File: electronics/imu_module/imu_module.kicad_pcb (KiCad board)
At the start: 2 copper layers, 30 x 40 mm, 26 parts, among them J1 Conn_01x06_Male, J2 Conn_01x04, J3 Conn_01x04, SW1 SW_Push, SW2 SW_Push, SW3 SW_Push, U1 ESP32-WROOM-32U, U2 SP485, U3 ISM330DHCXTR, U4 SN74LV1T34DBVR, U5 AP2114HA-3.3TRG1

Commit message: hacky
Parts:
- removed the C4 at (19.0, 20.5)
- removed the C5 at (18.5, 16.0)
- removed the C8 at (26.0, 9.00)
- removed SW1, SW2, SW3: SW_Push, Button_Switch_SMD:SW_SPST_B3S-1000
- removed the U3 at (26.0, 15.0)
- added C1: 100n, Capacitor_SMD:C_0805_2012Metric, F.Cu at (22.2, 12.9)
- added C3: 100n, Capacitor_SMD:C_0805_2012Metric, F.Cu at (28.6, 13.8)
- added C6: 10u/50V, Capacitor_SMD:C_1206_3216Metric, B.Cu at (9.53, 24.5)
- added C9: 22u/16v, Capacitor_SMD:C_1206_3216Metric, B.Cu at (20.2, 5.00)
- added D1: WS2812B, lib:LED_WS2812B_PLCC4_5.0x5.0mm_P3.2mm_marked, B.Cu at (5.50, 30.0)
- added D2: WS2812B, lib:LED_WS2812B_PLCC4_5.0x5.0mm_P3.2mm_marked, B.Cu at (15.0, 30.0)
- added D3: WS2812B, lib:LED_WS2812B_PLCC4_5.0x5.0mm_P3.2mm_marked, B.Cu at (24.5, 30.0)
- added G***: LOGO, bitbots:bitbots_logo, B.Cu at (21.8, 12.3)
- added J2: Conn_01x03_Male, Connector_PinHeader_2.54mm:PinHeader_1x03_P2.54mm_Vertical, F.Cu at (28.0, 18.9)
- added JP1: SolderJumper_2_Open, Jumper:SolderJumper-2_P1.3mm_Open_RoundedPad1.0x1.5mm, F.Cu at (25.4, 9.60)
- added L1: 22uH, lib:VLS5045EX330M, B.Cu at (15.0, 4.70)
- added R2: 4K7, Resistor_SMD:R_0805_2012Metric, F.Cu at (8.59, 32.5)
- added R3: 4K7, Resistor_SMD:R_0805_2012Metric, F.Cu at (4.84, 32.5)
- added U2: BMI088, lib:PQFN50P450X300X100-16N, F.Cu at (25.4, 13.5)
- C10: renamed from C9; footprint Capacitor_SMD:C_0805_2012Metric_Pad1.15x1.40mm_HandSolder -> Capacitor_SMD:C_1206_3216Metric; moved to B.Cu
- C11: renamed from C10; footprint Capacitor_SMD:C_0805_2012Metric_Pad1.15x1.40mm_HandSolder -> Capacitor_SMD:C_1206_3216Metric; moved to B.Cu
- C2: renamed from C1; footprint Capacitor_SMD:C_0805_2012Metric_Pad1.15x1.40mm_HandSolder -> Capacitor_SMD:C_0805_2012Metric
- C4: renamed from C2; footprint Capacitor_SMD:C_0805_2012Metric_Pad1.15x1.40mm_HandSolder -> Capacitor_SMD:C_0805_2012Metric
- C5: renamed from C3; footprint Capacitor_SMD:C_0805_2012Metric_Pad1.15x1.40mm_HandSolder -> Capacitor_SMD:C_0805_2012Metric
- C7: value 100n -> 22u/16v; footprint Capacitor_SMD:C_0805_2012Metric_Pad1.15x1.40mm_HandSolder -> Capacitor_SMD:C_1206_3216Metric
- C8: renamed from C6; footprint Capacitor_SMD:C_0805_2012Metric_Pad1.15x1.40mm_HandSolder -> Capacitor_SMD:C_0805_2012Metric
- PS1: value VXO7805-500-M -> PXO7805-500-M-TR; footprint bitbots:VXO7805-500-M -> lib:CONV_PXO7805-500-M-TR
- R1: footprint Resistor_SMD:R_0805_2012Metric_Pad1.15x1.40mm_HandSolder -> Resistor_SMD:R_0805_2012Metric
- U5: moved to B.Cu
- moved C7 21.4 mm to (9.75, 5.00), turned to 90 degrees
- moved J1 15.8 mm to (17.7, 28.0), turned to 180 degrees
- moved C11 10.5 mm to (15.5, 24.8), turned to 90 degrees
- moved J4 8.16 mm to (10.2, 36.5), turned to 180 degrees
- moved C10 8.15 mm to (21.0, 17.6), turned to 180 degrees
- moved C5 7.57 mm to (17.5, 4.20), turned to 90 degrees
- moved U5 7.56 mm to (21.2, 22.9), turned to 180 degrees
- moved J3 7.49 mm to (27.4, 36.5), turned to 180 degrees
- moved C2 6.67 mm to (13.4, 2.75)
- moved C4 4.10 mm to (20.0, 4.20), turned to 90 degrees
- moved R1 3.51 mm to (13.3, 5.25), turned to 180 degrees
- moved PS1 2.06 mm to (9.35, 15.6)
- moved U3 1.95 mm to (23.7, 23.7), turned to 180 degrees
- moved U1 1.61 mm to (11.1, 16.8), turned to -90 degrees
- moved C8 1.50 mm to (22.5, 30.0), turned to -90 degrees
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- renumbered J2 to J3, J3 to J4, U4 to U3, U2 to U4
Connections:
- C7 pad 1: +3V3 -> Net-(PS1-+VO)
- J3 pad 1: GND -> DATA-
- J3 pad 2: +1V2 -> DATA+
- J3 pad 3: DATA+ -> VBUS
- J3 pad 4: DATA- -> GND
- J4 pad 1: GND -> DATA-
- J4 pad 2: +1V2 -> DATA+
- J4 pad 3: DATA+ -> VBUS
- J4 pad 4: DATA- -> GND
- PS1 pad 1: +1V2 -> VBUS
- PS1 pad 2: GND -> (no net)
- PS1 pad 3: +5V -> Net-(PS1-+VO)
- PS1 pad 4: Net-(PS1-Pad4) -> GND
- U1 pad 10: Net-(U1-Pad10) -> int1_accel
- U1 pad 11: Net-(U1-Pad11) -> SPI_CS_ACCEL
- U1 pad 12: Net-(U1-Pad12) -> unconnected-(U1-IO27-Pad12)
- U1 pad 13: INT_ACC -> unconnected-(U1-IO14-Pad13)
- U1 pad 14: Net-(U1-Pad14) -> unconnected-(U1-IO12-Pad14)
- U1 pad 16: INT_GYR -> unconnected-(U1-IO13-Pad16)
- U1 pad 17: Net-(U1-Pad17) -> unconnected-(U1-SHD/SD2-Pad17)
- U1 pad 18: Net-(U1-Pad18) -> unconnected-(U1-SWP/SD3-Pad18)
- U1 pad 19: Net-(U1-Pad19) -> unconnected-(U1-SCS/CMD-Pad19)
- U1 pad 20: Net-(U1-Pad20) -> unconnected-(U1-SCK/CLK-Pad20)
- U1 pad 21: Net-(U1-Pad21) -> unconnected-(U1-SDO/SD0-Pad21)
- U1 pad 22: Net-(U1-Pad22) -> unconnected-(U1-SDI/SD1-Pad22)
- U1 pad 23: TX_EN -> SW2
- U1 pad 24: Net-(U1-Pad24) -> SW1
- U1 pad 26: Net-(U1-Pad26) -> LED
- U1 pad 27: U2_RX -> int3_gyro
- U1 pad 28: U2_TX -> SPI1_MISO
- U1 pad 29: SPI_CS -> SPI1_MOSI
- U1 pad 30: SPI1_SCK -> SPI_CS_GYRO
- U1 pad 31: SPI1_MISO -> SPI1_SCK
- U1 pad 32: Net-(U1-Pad32) -> unconnected-(U1-NC-Pad32)
- U1 pad 33: Net-(U1-Pad33) -> U2_RX
- U1 pad 36: Net-(U1-Pad36) -> TX_EN
- U1 pad 37: SPI1_MOSI -> U2_TX
- U1 pad 4: Net-(U1-Pad4) -> unconnected-(U1-SENSOR_VP-Pad4)
- U1 pad 5: Net-(U1-Pad5) -> unconnected-(U1-SENSOR_VN-Pad5)
- U1 pad 6: Net-(U1-Pad6) -> unconnected-(U1-IO34-Pad6)
- U1 pad 7: Net-(U1-Pad7) -> unconnected-(U1-IO35-Pad7)
- U1 pad 8: Net-(U1-Pad8) -> unconnected-(U1-IO32-Pad8)
- U1 pad 9: Net-(U1-Pad9) -> unconnected-(U1-IO33-Pad9)
- U3 pad 1: Net-(U4-Pad1) -> unconnected-(U3-NC-Pad1)
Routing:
- net GND: track 0.00 -> 82.4 mm, vias 0 -> 12
- net +3V3: track 0.00 -> 69.7 mm, vias 0 -> 5
- net DATA-: track 0.00 -> 47.1 mm
- net VBUS: track 0.00 -> 37.0 mm
- net en: track 0.00 -> 33.5 mm, vias 0 -> 2
- net SW1: track 0.00 -> 28.3 mm, vias 0 -> 1
- net SW2: track 0.00 -> 27.3 mm, vias 0 -> 1
- net SPI1_MISO: track 0.00 -> 26.6 mm
- net int3_gyro: track 0.00 -> 25.5 mm
- net +5V: track 0.00 -> 25.1 mm, vias 0 -> 6
- net DATA+: track 0.00 -> 24.6 mm
- net SPI_CS_GYRO: track 0.00 -> 23.3 mm
- net SPI1_MOSI: track 0.00 -> 21.6 mm
- net SPI_CS_ACCEL: track 0.00 -> 20.8 mm
- net SPI1_SCK: track 0.00 -> 20.0 mm
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- added copper zone on In2.Cu, net +5V
- added copper zone on In1.Cu, net GND
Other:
- copper layers 2 -> 4
- net class Default removed
- board text added: "+"
- board text added: "-"
- board text added: "BOOT"
- board text added: "EN"
- board text added: "IMU v2.0"
- board text added: "RX"
- board text added: "TX"
- board text added: "jasper@bit-bots.de"

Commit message: library updates
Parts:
- removed PS1: PXO7805-500-M-TR, lib:CONV_PXO7805-500-M-TR
- added PS2: PXO7805-500-M-TR, lib:PXO7805-500-M-TR, B.Cu at (9.23, 15.6)
- J1: footprint bitbots:testpoint_01x06 -> bitbots:esp32_pogo_programmer
- L1: value 22uH -> VLS5045EX-220M
- U2: footprint lib:PQFN50P450X300X100-16N -> lib:BMI088
- U3: value SN74LV1T34DBVR -> SN74LV1T34DBV; footprint bitbots:SN74LV1T34DBVR -> Package_TO_SOT_SMD:SOT-23-5
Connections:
- J1 pad 1: +3V3 -> +5V
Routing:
- net +3V3: track 69.7 -> 65.7 mm, vias 5 -> 4
- net +5V: track 25.1 -> 27.2 mm

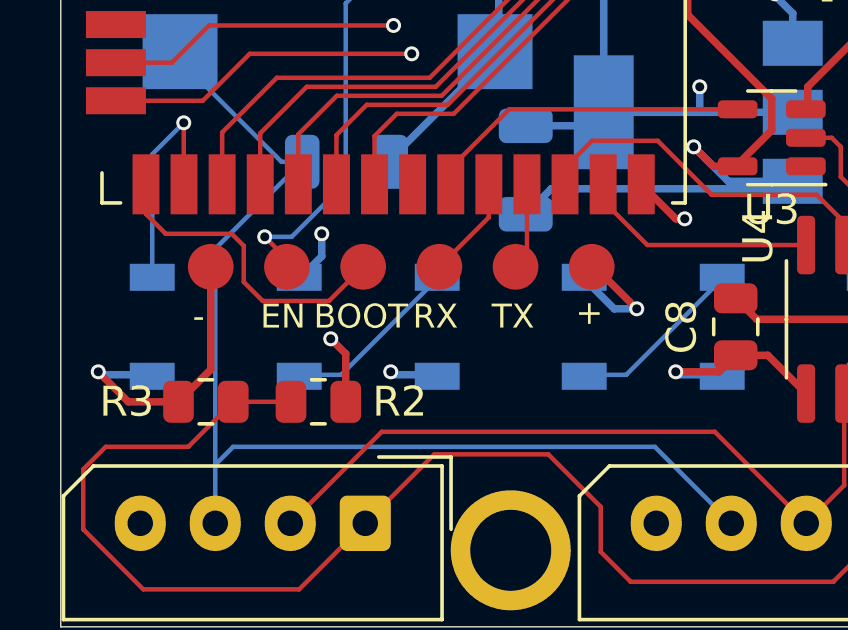
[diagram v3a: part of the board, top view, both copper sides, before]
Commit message: more cleanup and 3d models
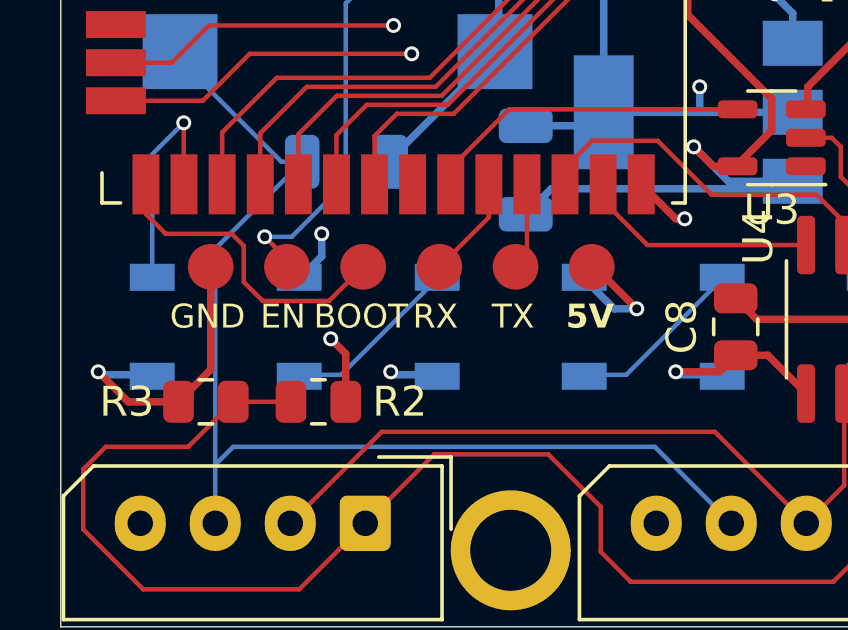
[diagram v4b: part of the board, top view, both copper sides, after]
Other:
- board text added: "5V"
- board text added: "GND"
- board text added: "IMU v2.1"
- board text removed: "+"
- board text removed: "IMU v2.0"
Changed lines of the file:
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@@
 			(pintype "bidirectional")
 		)
+		(model "${KIPRJMOD}/lib/BMI088.step"
+			(offset
+				(xyz 0 0 0)
+			)
+			(scale
+				(xyz 1 1 1)
+			)
+			(rotate
+				(xyz -90 0 0)
+			)
+		)
 	)
 	(footprint "Resistor_SMD:R_0805_2012Metric"
@@
 		(tags "Inductor")
 		(property "Reference" "L1"
-			(at -0.014 -3.43 360)
+			(at -0.014 -3.43 0)
 			(layer "B.SilkS")
 			(effects
@@
 		)
 		(property "Value" "VLS5045EX-220M"
-			(at 0 0 360)
+			(at 0 0 0)
 			(layer "B.SilkS")
 			(hide yes)
@@
 		)
 		(fp_text user "${REFERENCE}"
-			(at 0 0 360)
+			(at 0 0 0)
 			(layer "B.Fab")
 			(effects
@@
 			(pintype "passive")
 		)
-		(model "VLS5045EX-220M.stp"
+		(model "${KIPRJMOD}/lib/VLS5045EX-220M.step"
 			(offset
-				(xyz 0 0 2.259999957)
+				(xyz 0 0 2.26)
 			)
 			(scale
@@
 		(at 9.228 15.578)
 		(property "Reference" "PS2"
-			(at -3.575 8.385 360)
+			(at -3.575 8.385 0)
 			(layer "B.SilkS")
 			(effects
@@
 		)
 		(property "Value" "PXO7805-500-M-TR"
-			(at 6.585 -8.385 360)
+			(at 6.585 -8.385 0)
 			(layer "B.Fab")
 			(effects
@@
 			(pintype "power_in")
 		)
+		(model "${KIPRJMOD}/lib/PXO7805-500-M-TR.step"
+			(offset
+				(xyz -6 6 0)
+			)
+			(scale
+				(xyz 1 1 1)
+			)
+			(rotate
+				(xyz -90 0 0)
+			)
+		)
 	)
 	(footprint "lib:LED_WS2812B_PLCC4_5.0x5.0mm_P3.2mm_marked"
@@
 		)
 	)
-	(gr_text "IMU\nv2.0"
+	(gr_text "IMU\nv2.1"
 		(at 27.2 8.1 0)
 		(layer "B.SilkS")
@@
 		)
 	)
-	(gr_text "+"
-		(at 17.159762 30 0)
+	(gr_text "5V"
+		(at 16.831191 30.125 0)
 		(layer "F.SilkS")
 		(effects
 			(font
 				(size 0.8 0.8)
-				(thickness 0.1)
+				(thickness 0.15)
+				(bold yes)
 			)
 			(justify left bottom)
@@
 		)
 	)
-	(gr_text "-"
-		(at 4.397262 30.125 0)
+	(gr_text "GND\n"
+		(at 3.635953 30.125 0)
 		(layer "F.SilkS")
 		(effects

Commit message: prep for production
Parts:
- J1: footprint bitbots:esp32_pogo_programmer -> lib:esp32_pogo_programmer
- moved J1 12.7 mm to (5.00, 28.0), turned to 0 degrees
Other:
- board text removed: "5V"
- board text removed: "BOOT"
- board text removed: "EN"
- board text removed: "GND"
- board text removed: "RX"
- board text removed: "TX"

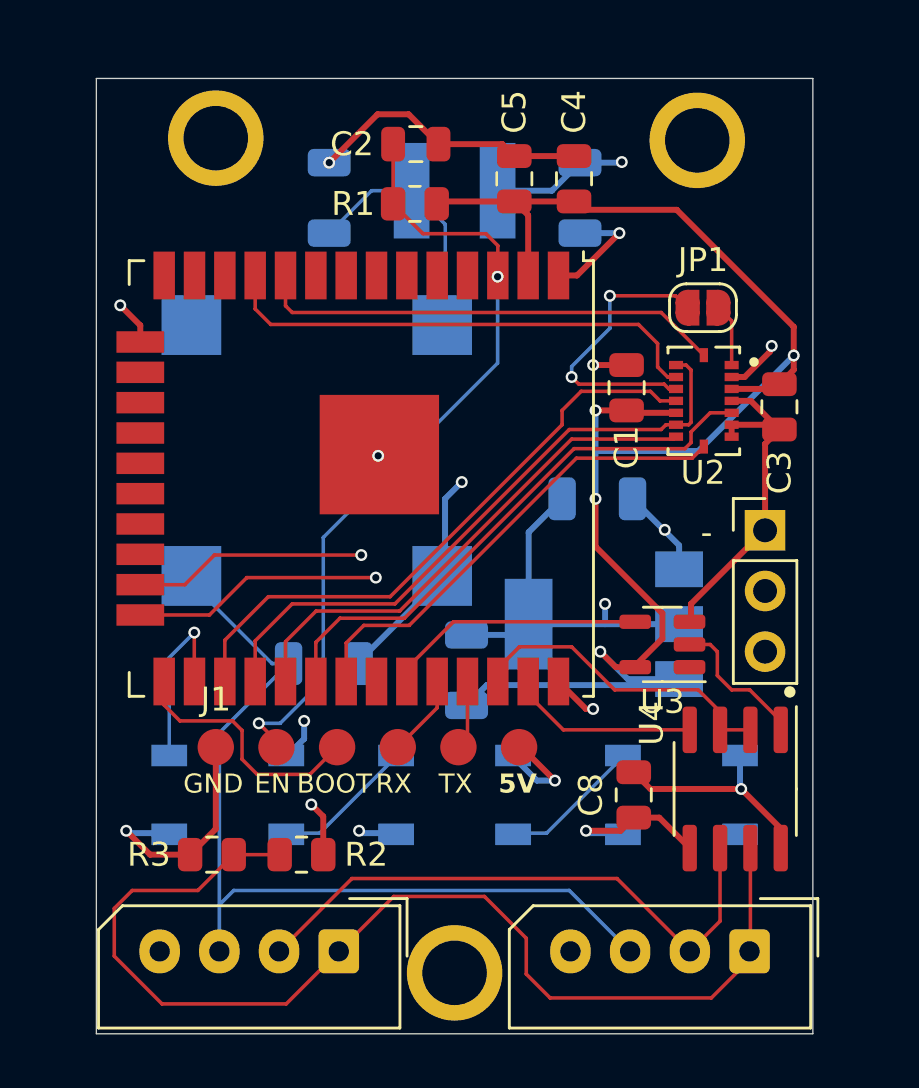
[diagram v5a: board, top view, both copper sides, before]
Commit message: new routing for buttons + leds on board
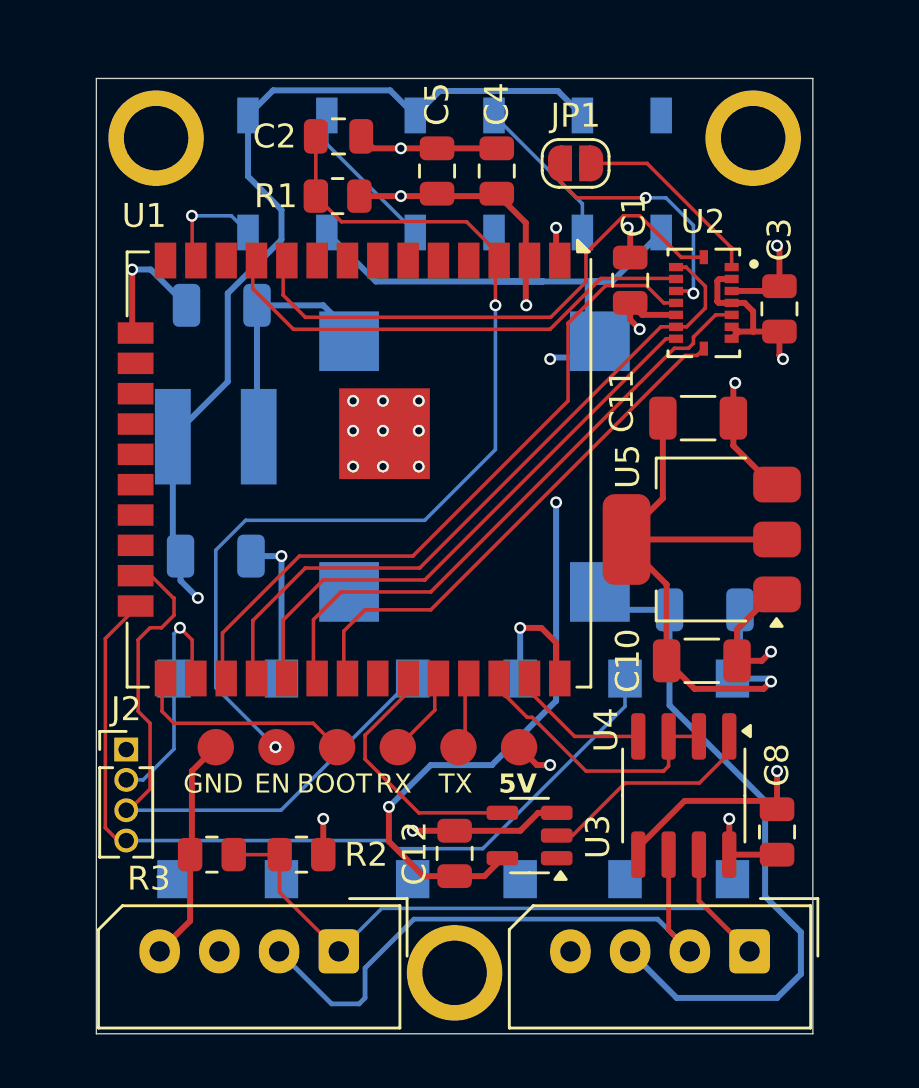
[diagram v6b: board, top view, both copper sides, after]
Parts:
- removed the G*** at (21.8, 12.3)
- added C12: 100n, Capacitor_SMD:C_0805_2012Metric, F.Cu at (15.0, 32.5)
- added G***: LOGO, lib:bitbots_logo7x8.7mm, B.Cu at (26.2, 14.2)
- added SW1: SW_Push, lib:RND 210-00211, B.Cu at (24.4, 29.3)
- added SW2: SW_Push, lib:RND 210-00211, B.Cu at (15.5, 29.3)
- added SW3: SW_Push, lib:RND 210-00211, B.Cu at (5.50, 29.3)
- C10, C11, U5: moved to F.Cu
- J2: value Conn_01x03_Male -> Conn_01x04_Pin; footprint Connector_PinHeader_2.54mm:PinHeader_1x03_P2.54mm_Vertical -> Connector_PinHeader_1.27mm:PinHeader_1x04_P1.27mm_Vertical
- U1: footprint RF_Module:ESP32-WROOM-32U -> RF_Module:ESP32-WROOM-32UE
- moved J2 28.3 mm to (1.25, 28.1)
- moved D1 26.1 mm to (8.00, 4.00), turned to -90 degrees
- moved D3 26.1 mm to (22.0, 4.00), turned to -90 degrees
- moved D2 26.0 mm to (15.0, 4.00), turned to -90 degrees
- moved C9 21.4 mm to (5.00, 20.0), turned to 0 degrees
- moved C6 16.1 mm to (25.5, 22.2)
- moved L1 14.4 mm to (5.00, 15.0), turned to 180 degrees
- moved C11 14.3 mm to (25.2, 14.2), turned to 180 degrees
- moved U3 9.74 mm to (18.1, 31.7)
- moved C10 8.07 mm to (25.4, 24.4)
- moved JP1 8.06 mm to (20.1, 3.56)
- moved PS2 6.64 mm to (15.8, 16.2), turned to 90 degrees
- moved C7 6.36 mm to (5.25, 9.50), turned to 180 degrees
- moved C8 6.20 mm to (28.5, 31.6), turned to 90 degrees
- moved U5 5.42 mm to (25.4, 19.3)
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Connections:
- net Net-(PS2-+VO) renamed /5V_reg_out
- J2 pad 2: SW2 -> SW3
- J2 pad 3: SW1 -> SW2
- U1 pad 13: unconnected-(U1-IO14-Pad13) -> LED
- U1 pad 26: LED -> SW3
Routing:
- net GND: track 82.4 -> 114.0 mm, vias 12 -> 20
- net +5V: track 27.2 -> 49.7 mm, vias 6 -> 5
- net +3V3: track 65.7 -> 47.4 mm, vias 4 -> 7
- net DATA-: track 47.1 -> 30.7 mm
- net SW3: track 0.00 -> 9.80 mm, vias 0 -> 1
- net en: track 33.5 -> 42.1 mm
- net VBUS: track 37.0 -> 28.8 mm
- net SW1: track 28.3 -> 35.6 mm, vias 1 -> 0
- net int2_accel: track 2.63 -> 8.15 mm
- net int3_gyro: track 25.5 -> 28.9 mm
- net rs485_rx: track 6.04 -> 9.35 mm
- net LED: track 7.69 -> 4.77 mm
- net int1_accel: track 19.6 -> 22.4 mm
- net SPI1_MISO: track 26.6 -> 29.0 mm
- net SPI1_MOSI: track 21.6 -> 23.5 mm
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- added copper zone on In2.Cu, net +3V3
- added copper zone on In2.Cu, net VBUS
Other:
- board text added: "rev2.1"
- board text removed: "-"
- board text removed: "IMU v2.1"

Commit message: production version and bom
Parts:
- removed G***: LOGO, lib:bitbots_logo7x8.7mm
- removed PS2: PXO7805-500-M-TR, lib:PXO7805-500-M-TR
- added PS1: VXO7803-500-M, lib:CONV_VXO7803-500-M, B.Cu at (16.9, 16.2)
- J1: value Conn_01x06_Male -> PRGM+Debug; footprint lib:esp32_pogo_programmer -> lib:esp32_prgm_debug
- moved R3 11.1 mm to (15.9, 32.5), turned to -90 degrees
- moved R2 8.20 mm to (15.9, 28.8), turned to -90 degrees
- moved C12 5.42 mm to (19.4, 29.2), turned to 0 degrees
- moved J1 4.07 mm to (8.34, 30.3)
- moved C6 2.00 mm to (27.5, 22.2)
- moved U3 1.12 mm to (19.2, 32.1)
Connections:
- J1 pad 6: GND -> JTAG_MTDO
- U1 pad 12: unconnected-(U1-IO27-Pad12) -> LED
- U1 pad 13: LED -> JTAG_MTMS
- U1 pad 14: unconnected-(U1-IO12-Pad14) -> JTAG_MTDI
- U1 pad 16: unconnected-(U1-IO13-Pad16) -> JTAG_MTCK
- U1 pad 23: SW2 -> JTAG_MTDO
- U1 pad 8: unconnected-(U1-IO32-Pad8) -> SW2
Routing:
- net JTAG_MTDI: track 0.00 -> 24.3 mm, vias 0 -> 2
- net JTAG_MTMS: track 0.00 -> 24.2 mm, vias 0 -> 2
- net JTAG_MTCK: track 0.00 -> 20.0 mm, vias 0 -> 2
- net JTAG_MTDO: track 0.00 -> 9.65 mm
- net GND: track 114.0 -> 105.5 mm, vias 20 -> 21
- net SW2: track 26.7 -> 34.8 mm, vias 0 -> 3
- net rx_esp: track 3.77 -> 9.99 mm
- net tx_esp: track 3.24 -> 8.88 mm
- net en: track 42.1 -> 45.3 mm
- net DATA-: track 30.7 -> 33.4 mm
- net +3V3: track 47.4 -> 49.4 mm, vias 7 -> 6
- net boot: track 9.58 -> 7.68 mm
- net LED: track 4.77 -> 2.92 mm
- net +5V: track 49.7 -> 51.3 mm, vias 5 -> 4
- net SW3: track 9.80 -> 8.60 mm
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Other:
- board text added: "IMU-DXL rev2"
